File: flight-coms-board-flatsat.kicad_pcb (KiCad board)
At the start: 4 copper layers, 69.1 x 72.5 mm, 50 parts, among them J2 Conn_02x05_Odd_Even, J3 Conn_02x10_Odd_Even, J4 Conn_02x10_Odd_Even, J5 CONSMA001-SMD-G, U1 CC1200, U2 TPS79330-EP, Y2 40MHz

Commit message: Minor fixes and changes
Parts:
- C15: value 36pF -> 39pF

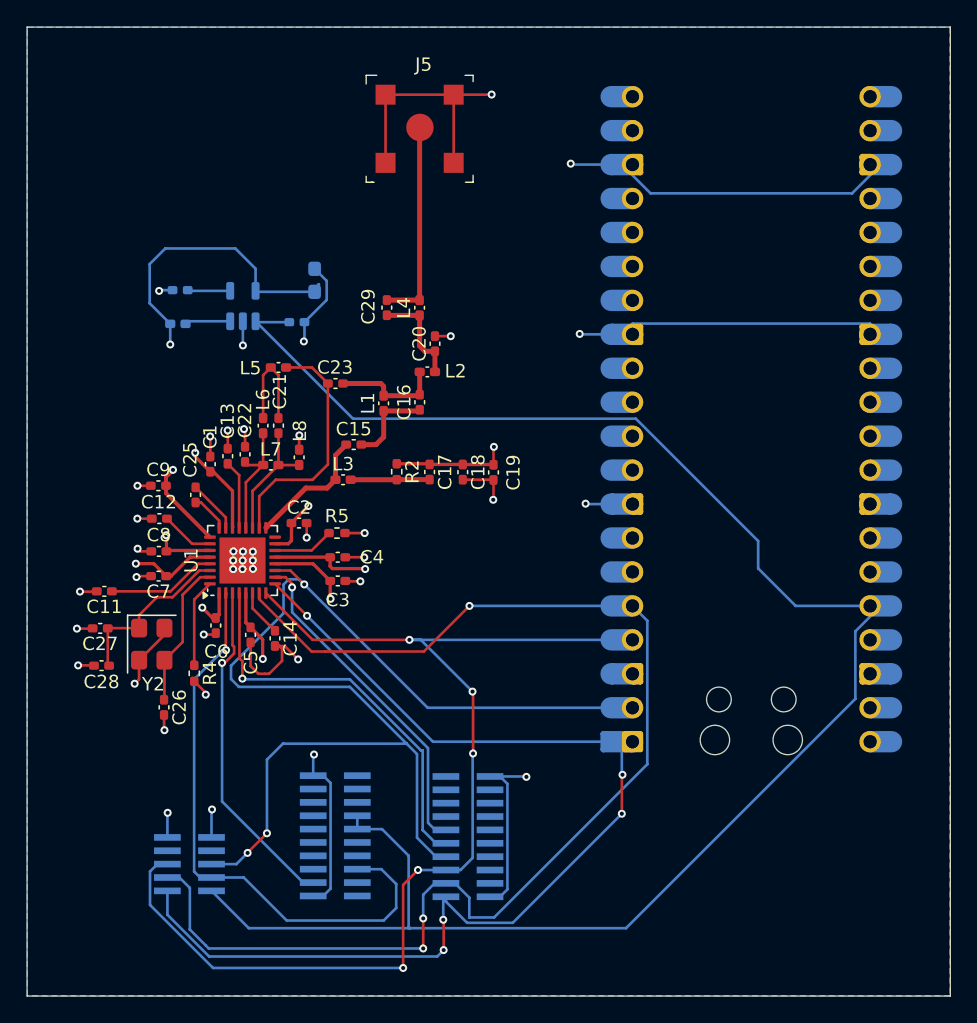
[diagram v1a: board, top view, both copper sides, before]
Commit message: Flipped pico footprint for USB clearance
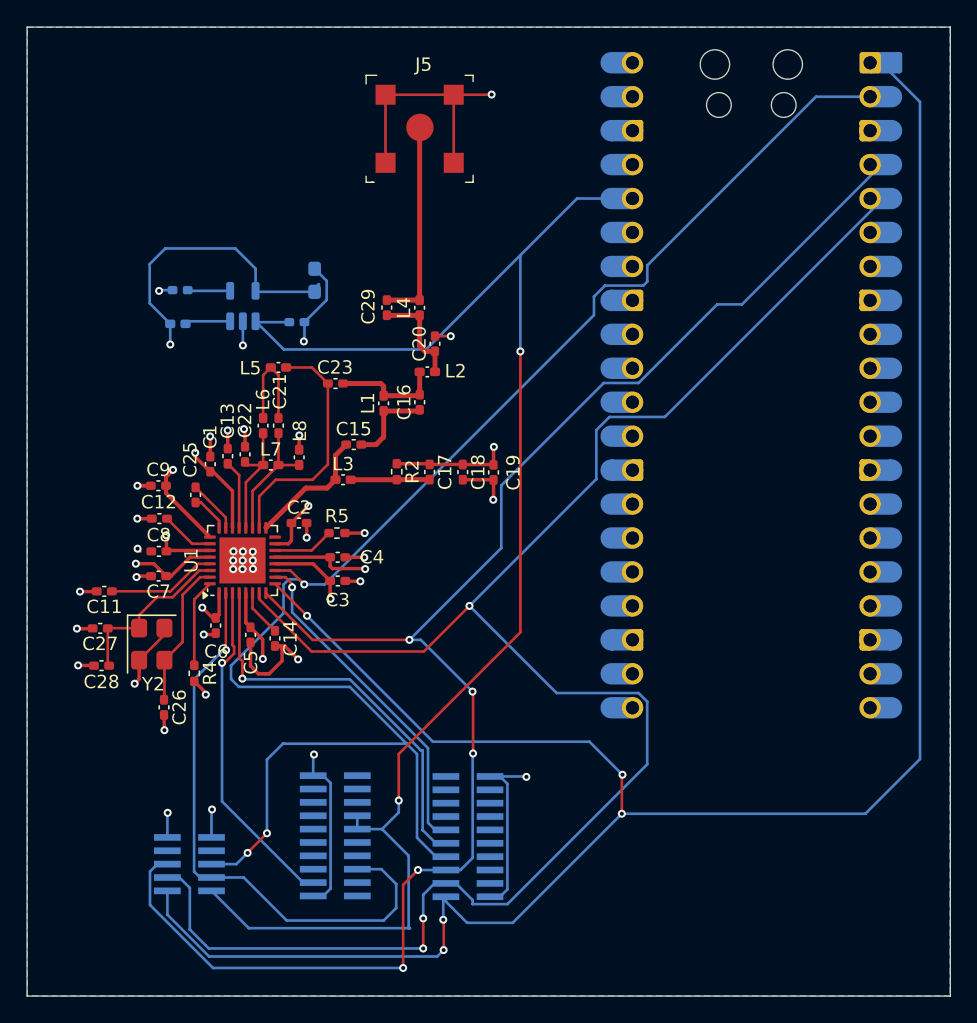
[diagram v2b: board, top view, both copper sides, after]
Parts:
- moved A1 2.54 mm to (178.1, 84.0), turned to 180 degrees
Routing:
- net /MISO: track 81.9 -> 157.8 mm
- net GND: track 152.7 -> 101.8 mm, vias 41 -> 38
- net /MOSI: track 93.9 -> 135.3 mm
- net /SCLK: track 84.1 -> 120.9 mm
- net /CSN: track 87.8 -> 120.0 mm
- net /3V3: track 134.7 -> 109.9 mm, vias 0 -> 2
